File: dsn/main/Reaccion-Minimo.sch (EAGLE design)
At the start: 43 parts, among them U1 ATMEGA328P_TQFP, U2 MIC5219 5V, Y1 16MHz

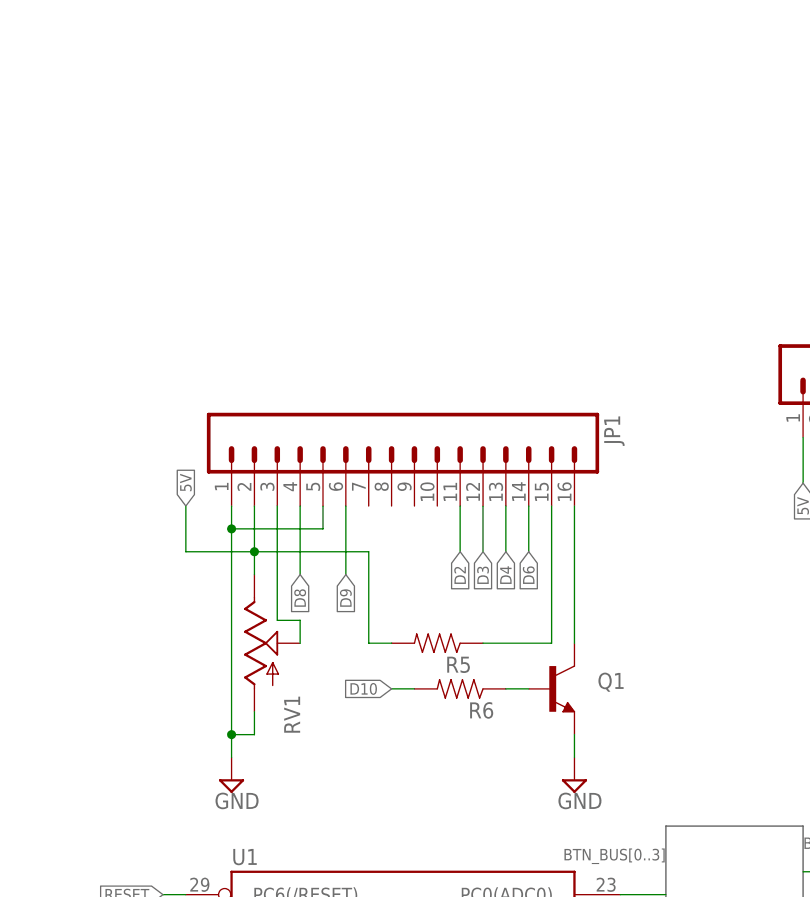
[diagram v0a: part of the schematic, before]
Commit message: Reaccion Minimo UI finished. RX send tested.
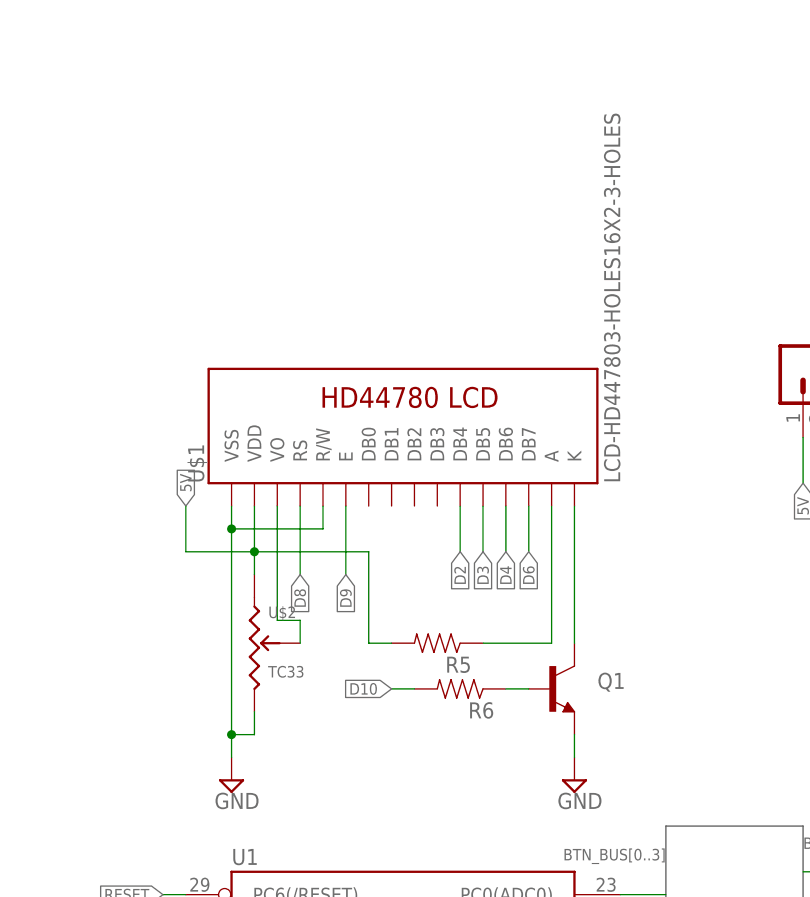
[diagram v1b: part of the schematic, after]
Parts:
- removed JP1: (no value), SparkFun-Connectors:M16PTH
- removed RV1: (no value), SparkFun-Electromechanical:POT-RV16AF-20
- added U$1: LCD-HD447803-HOLES16X2-3-HOLES, HD44780LCD:LCD-HD447803-HOLES16X2-3-HOLES
- added U$2: TC33, Reaccion-Minimo:TC33
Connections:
- net 5V: now also U$1.VDD, U$2.1; no longer JP1.2, RV1.E
- net D2: now also U$1.DB4; no longer JP1.11
- net D3: now also U$1.DB5; no longer JP1.12
- net D4: now also U$1.DB6; no longer JP1.13
- net D6: now also U$1.DB7; no longer JP1.14
- net D8: now also U$1.RS; no longer JP1.4
- net D9: now also U$1.E; no longer JP1.6
- net GND: now also U$1.R/W, U$1.VSS, U$2.3; no longer JP1.1, JP1.5, RV1.A
- net N$6: now also U$1.A; no longer JP1.15
- net N$7: now also U$1.VO, U$2.2; no longer JP1.3, RV1.S
- net N$8: now also U$1.K; no longer JP1.16
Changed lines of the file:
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@@
 <part name="S3" library="SparkFun-Electromechanical" deviceset="SWITCH-MOMENTARY-2" device="SMD"/>
 <part name="S4" library="SparkFun-Electromechanical" deviceset="SWITCH-MOMENTARY-2" device="SMD"/>
-<part name="JP1" library="SparkFun-Connectors" deviceset="M16" device="PTH"/>
 <part name="TX_MOD_CONN" library="SparkFun-Connectors" deviceset="M04" device="PTH"/>
 <part name="JP6" library="SparkFun-Connectors" deviceset="POWER_JACK" device="PTH"/>
@@
 <part name="SUPPLY1" library="supply2" deviceset="GND" device=""/>
 <part name="ISP1" library="adafruit" deviceset="AVRISP" device="-6"/>
-<part name="RV1" library="SparkFun-Electromechanical" deviceset="POT" device="-RV16AF-20"/>
 <part name="SUPPLY2" library="supply2" deviceset="GND" device=""/>
 <part name="SUPPLY3" library="supply2" deviceset="GND" device=""/>
@@
 <part name="C7" library="SparkFun-Capacitors" deviceset="CAP" device="0805"/>
 <part name="C8" library="SparkFun-Capacitors" deviceset="CAP" device="0805"/>
+<part name="U$1" library="HD44780LCD" deviceset="LCD-HD44780" device="16X2-3-HOLES" technology="3-HOLES"/>
+<part name="U$2" library="Reaccion-Minimo" deviceset="TC33" device=""/>
 </parts>
 <sheets>
@@
 <instance part="S3" gate="G$1" x="139.7" y="53.34"/>
 <instance part="S4" gate="G$1" x="139.7" y="45.72"/>
-<instance part="JP1" gate="G$1" x="86.36" y="119.38" rot="R270"/>
 <instance part="TX_MOD_CONN" gate="G$1" x="170.18" y="104.14" rot="R270"/>
 <instance part="JP6" gate="G$1" x="-40.64" y="106.68"/>
@@
 <instance part="SUPPLY1" gate="GND" x="-35.56" y="101.6"/>
 <instance part="ISP1" gate="G$1" x="-15.24" y="45.72"/>
-<instance part="RV1" gate="G$1" x="68.58" y="93.98"/>
 <instance part="SUPPLY2" gate="GND" x="7.62" y="93.98"/>
 <instance part="SUPPLY3" gate="GND" x="58.42" y="5.08"/>
@@
 <instance part="C7" gate="G$1" x="2.54" y="109.22" rot="R180"/>
 <instance part="C8" gate="G$1" x="30.48" y="109.22" rot="R180"/>
+<instance part="U$1" gate="G$1" x="86.36" y="119.38" rot="R90"/>
+<instance part="U$2" gate="G$1" x="68.58" y="93.98"/>
 </instances>
 <busses>
@@
 </segment>
 <segment>
-<pinref part="JP1" gate="G$1" pin="2"/>
 <wire x1="68.58" y1="109.22" x2="68.58" y2="104.14" width="0.1524" layer="91"/>
 <wire x1="68.58" y1="104.14" x2="60.96" y2="104.14" width="0.1524" layer="91"/>
 <wire x1="60.96" y1="104.14" x2="60.96" y2="109.22" width="0.1524" layer="91"/>
 <label x="60.96" y="109.22" size="1.27" layer="95" rot="R90" xref="yes"/>
-<pinref part="RV1" gate="G$1" pin="E"/>
 <wire x1="68.58" y1="104.14" x2="68.58" y2="101.6" width="0.1524" layer="91"/>
 <junction x="68.58" y="104.14"/>
@@
 <pinref part="R5" gate="G$1" pin="2"/>
 <wire x1="81.28" y1="93.98" x2="83.82" y2="93.98" width="0.1524" layer="91"/>
+<pinref part="U$1" gate="G$1" pin="VDD"/>
+<pinref part="U$2" gate="G$1" pin="1"/>
 </segment>
 <segment>
@@
 </segment>
 <segment>
-<pinref part="JP1" gate="G$1" pin="1"/>
 <pinref part="SUPPLY9" gate="GND" pin="GND"/>
 <wire x1="66.04" y1="109.22" x2="66.04" y2="106.68" width="0.1524" layer="91"/>
-<pinref part="JP1" gate="G$1" pin="5"/>
 <wire x1="66.04" y1="106.68" x2="66.04" y2="83.82" width="0.1524" layer="91"/>
 <wire x1="66.04" y1="83.82" x2="66.04" y2="81.28" width="0.1524" layer="91"/>
@@
 <wire x1="76.2" y1="106.68" x2="66.04" y2="106.68" width="0.1524" layer="91"/>
 <junction x="66.04" y="106.68"/>
-<pinref part="RV1" gate="G$1" pin="A"/>
 <wire x1="68.58" y1="86.36" x2="68.58" y2="83.82" width="0.1524" layer="91"/>
 <wire x1="68.58" y1="83.82" x2="66.04" y2="83.82" width="0.1524" layer="91"/>
 <junction x="66.04" y="83.82"/>
+<pinref part="U$1" gate="G$1" pin="R/W"/>
+<pinref part="U$1" gate="G$1" pin="VSS"/>
+<pinref part="U$2" gate="G$1" pin="3"/>
 </segment>
 <segment>
@@
 </segment>
 <segment>
-<pinref part="JP1" gate="G$1" pin="11"/>
 <wire x1="91.44" y1="109.22" x2="91.44" y2="104.14" width="0.1524" layer="91"/>
 <label x="91.44" y="104.14" size="1.27" layer="95" rot="R270" xref="yes"/>
+<pinref part="U$1" gate="G$1" pin="DB4"/>
 </segment>
 </net>
@@
 </segment>
 <segment>
-<pinref part="JP1" gate="G$1" pin="12"/>
 <wire x1="93.98" y1="109.22" x2="93.98" y2="104.14" width="0.1524" layer="91"/>
 <label x="93.98" y="104.14" size="1.27" layer="95" rot="R270" xref="yes"/>
+<pinref part="U$1" gate="G$1" pin="DB5"/>
 </segment>
 </net>
@@
 </segment>
 <segment>
-<pinref part="JP1" gate="G$1" pin="13"/>
 <wire x1="96.52" y1="109.22" x2="96.52" y2="104.14" width="0.1524" layer="91"/>
 <label x="96.52" y="104.14" size="1.27" layer="95" rot="R270" xref="yes"/>
+<pinref part="U$1" gate="G$1" pin="DB6"/>
 </segment>
 </net>
@@
 </segment>
 <segment>
-<pinref part="JP1" gate="G$1" pin="14"/>
 <wire x1="99.06" y1="109.22" x2="99.06" y2="104.14" width="0.1524" layer="91"/>
 <label x="99.06" y="104.14" size="1.27" layer="95" rot="R270" xref="yes"/>
+<pinref part="U$1" gate="G$1" pin="DB7"/>
 </segment>
 </net>
@@
 </segment>
 <segment>
-<pinref part="JP1" gate="G$1" pin="6"/>
 <wire x1="78.74" y1="109.22" x2="78.74" y2="101.6" width="0.1524" layer="91"/>
 <label x="78.74" y="101.6" size="1.27" layer="95" rot="R270" xref="yes"/>
+<pinref part="U$1" gate="G$1" pin="E"/>
 </segment>
 </net>
@@
 </segment>
 <segment>
-<pinref part="JP1" gate="G$1" pin="4"/>
 <wire x1="73.66" y1="109.22" x2="73.66" y2="101.6" width="0.1524" layer="91"/>
 <label x="73.66" y="101.6" size="1.27" layer="95" rot="R270" xref="yes"/>
+<pinref part="U$1" gate="G$1" pin="RS"/>
 </segment>
 </net>
 <net name="N$7" class="0">
 <segment>
-<pinref part="RV1" gate="G$1" pin="S"/>
 <wire x1="73.66" y1="93.98" x2="73.66" y2="96.52" width="0.1524" layer="91"/>
-<pinref part="JP1" gate="G$1" pin="3"/>
 <wire x1="73.66" y1="96.52" x2="71.12" y2="96.52" width="0.1524" layer="91"/>
 <wire x1="71.12" y1="96.52" x2="71.12" y2="109.22" width="0.1524" layer="91"/>
+<pinref part="U$1" gate="G$1" pin="VO"/>
+<pinref part="U$2" gate="G$1" pin="2"/>
 </segment>
 </net>
@@
 <segment>
 <pinref part="R5" gate="G$1" pin="1"/>
-<pinref part="JP1" gate="G$1" pin="15"/>
 <wire x1="93.98" y1="93.98" x2="101.6" y2="93.98" width="0.1524" layer="91"/>
 <wire x1="101.6" y1="93.98" x2="101.6" y2="109.22" width="0.1524" layer="91"/>
+<pinref part="U$1" gate="G$1" pin="A"/>
 </segment>
 </net>
@@
 <segment>
 <pinref part="Q1" gate="G$1" pin="C"/>
-<pinref part="JP1" gate="G$1" pin="16"/>
 <wire x1="104.14" y1="93.98" x2="104.14" y2="109.22" width="0.1524" layer="91"/>
-</segment>
-</net>
+<pinref part="U$1" gate="G$1" pin="K"/>
+</segment>
+</net>

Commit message: Added Reaccion-Minimo PASTO
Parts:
- removed D4: GREEN, SparkFun-LED:LED-GREEN1206
- added C9: 1uF, SparkFun-Capacitors:CAP0805
- added U3: WS2811, SparkFun-LED:LED-TRICOLOR-5050-ICWS2811
- C1, C2: value (none) -> 18pF
- C3, C7: value (none) -> 1uF
- C4: value (none) -> 0.1uF
- C6: value (none) -> 100uF
- C8: value (none) -> 4.7uF
- R1, R6, R8: value (none) -> 4.7K
- R2: value (none) -> 150
- R3, R4: value (none) -> 330
- R5: value (none) -> 0
- U2: value MIC5219 5V -> lp2992aim5-5.0
- renumbered S5 to RESET, U$1 to LCD
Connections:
- net 5V: now also C9.2, U3.VDD; no longer R2.2
- net GND: now also C9.1, U3.VSS
- net HEARTBEAT: now also R2.2; no longer D4.C
- net N$3: now also U3.DI; no longer D4.A
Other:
- moved on the sheet: C5, C6, C7, C8, D1, D7, JP6, R2, R7, R9, U2
